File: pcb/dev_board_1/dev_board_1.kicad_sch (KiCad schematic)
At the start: 54 parts, among them SW1 SW_DIP_x01, SW10 SW_DIP_x01, SW11 SW_DIP_x01, SW12 SW_DIP_x01, SW13 SW_DIP_x01, SW14 SW_DIP_x01, SW15 SW_DIP_x01, SW16 SW_DIP_x01, SW17 SW_DIP_x01, SW18 SW_DIP_x01, SW19 SW_DIP_x01, SW2 SW_DIP_x01, SW20 SW_DIP_x01, SW21 SW_DIP_x01, SW22 SW_DIP_x01, SW23 SW_DIP_x01, SW24 SW_DIP_x01, SW3 SW_DIP_x01, SW4 SW_DIP_x01, SW5 SW_DIP_x01, SW6 SW_DIP_x01, SW7 SW_DIP_x01, SW8 SW_DIP_x01, SW9 SW_DIP_x01, U1 ili9341_touch_3.2, U2 LD3985M33R_SOT23, U3 STM32F427ZGTx, U4 MT48LC16M16A2TG

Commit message: add display
Add ili9341 display whit parallel interface
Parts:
- added SW25, SW26: SW_Push, Button_Switch_SMD:SW_SPST_SKQG_WithoutStem, symbol Switch:SW_Push
- added U5: ~, my_lib:ili9486_16bit_3.2, symbol my_lib:ili9341_touch_sd_16bit
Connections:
- net +3.3V: now also U3.108 (VDD), U3.121 (VDD), U3.131 (VDD), U3.144 (VDD), U3.17 (VDD), U3.30 (VDD), U3.33 (VDDA), U3.39 (VDD), U3.52 (VDD), U3.62 (VDD), U3.72 (VDD), U3.84 (VDD), U3.95 (VDD), U4.1 (VDD), U4.14 (VDD), U4.27 (VDD), U4.3 (VDDQ), U4.43 (VDDQ), U4.49 (VDDQ), U4.9 (VDDQ), U5.24 (VCC), U5.25 (VCC)
- net GND: now also U3.107 (VSS), U3.120 (VSS), U3.130 (VSS), U3.16 (VSS), U3.31 (VSSA), U3.38 (VSS), U3.51 (VSS), U3.61 (VSS), U3.83 (VSS), U3.94 (VSS), U4.12 (VSSQ), U4.28 (VSS), U4.41 (VSS), U4.46 (VSSQ), U4.52 (VSSQ), U4.54 (VSS), U4.6 (VSSQ), U5.26 (GND), U5.27 (GND)
- net cs_touch: now also U5.33 (~{CS_touch}); no longer U1.11 (~{CS_touch})
- net irg_touch: no longer U1.14 (IRQ_touch)
- net miso_touch: now also U5.29 (MISO_touch); no longer U1.13 (MISO_touch)
- net mosi_touch: now also U5.30 (MOSI_touch); no longer U1.12 (MOSI_touch)
- net sck_touch: now also U5.34 (SCK_touch); no longer U1.10 (SCK_touch)
- net FMC_NOE: now reaches U3.118 (PD4)
- net FMC_NOE: now also U5.4 (RD)
- net FMC_NWE: now reaches U3.119 (PD5)
- net FMC_NWE: now also U5.3 (WR)
- net FMC_NE1: now reaches U3.123 (PD7)
- net FMC_NE1: now also U5.1 (~{CS_display})
- net FMC_A16: now reaches U3.80 (PD11)
- net FMC_A16: now also U5.2 (D/~{C}_display)
- net sdram_A0 renamed FMC_A0
- net sdram_A1 renamed FMC_A1
- net sdram_A10 renamed FMC_A10
- net sdram_A11 renamed FMC_A11
- net sdram_A12 renamed FMC_A12
- net sdram_A2 renamed FMC_A2
- net sdram_A3 renamed FMC_A3
- net sdram_A4 renamed FMC_A4
- net sdram_A5 renamed FMC_A5
- net sdram_A6 renamed FMC_A6
- net sdram_A7 renamed FMC_A7
- net sdram_A8 renamed FMC_A8
- net sdram_A9 renamed FMC_A9
- net sdram_BA0 renamed FMC_BA0
- net sdram_BA1 renamed FMC_BA1
- net sdram_CKE renamed FMC_CKE
- net sdram_CLK renamed FMC_CLK
- net sdram_D0 renamed FMC_D0
- net FMC_D0: now also U5.6 (DB0)
- net sdram_D1 renamed FMC_D1
- net FMC_D1: now also U5.7 (DB1)
- net sdram_D10 renamed FMC_D10
- net FMC_D10: now also U5.16 (DB10)
- net sdram_D11 renamed FMC_D11
- net FMC_D11: now also U5.17 (DB11)
- net sdram_D12 renamed FMC_D12
- net FMC_D12: now also U5.18 (DB12)
- net sdram_D13 renamed FMC_D13
- net FMC_D13: now also U5.19 (DB13)
- net sdram_D14 renamed FMC_D14
- net FMC_D14: now also U5.20 (DB14)
- net sdram_D15 renamed FMC_D15
- net FMC_D15: now also U5.21 (DB15)
- net sdram_D2 renamed FMC_D2
- net FMC_D2: now also U5.8 (DB2)
- net sdram_D3 renamed FMC_D3
- net FMC_D3: now also U5.9 (DB3)
- net sdram_D4 renamed FMC_D4
- net FMC_D4: now also U5.10 (DB4)
- net sdram_D5 renamed FMC_D5
- net FMC_D5: now also U5.11 (DB5)
- net sdram_D6 renamed FMC_D6
- net FMC_D6: now also U5.12 (DB6)
- net sdram_D7 renamed FMC_D7
- net FMC_D7: now also U5.13 (DB7)
- net sdram_D8 renamed FMC_D8
- net FMC_D8: now also U5.14 (DB8)
- net sdram_D9 renamed FMC_D9
- net FMC_D9: now also U5.15 (DB9)
- net sdram_DQMH renamed FMC_DQMH
- net sdram_DQML renamed FMC_DQML
- net sdram_~{CAS} renamed FMC_~{CAS}
- net sdram_~{CS} renamed FMC_~{CS}
- net sdram_~{RAS} renamed FMC_~{RAS}
- net sdram_~{WE} renamed FMC_~{WE}
- new net LCD_LED: U5.23 (LED)
- new net LCD_RESET: U5.5 (RESET)
- new net irq_touch: U5.31 (IRQ_touch)

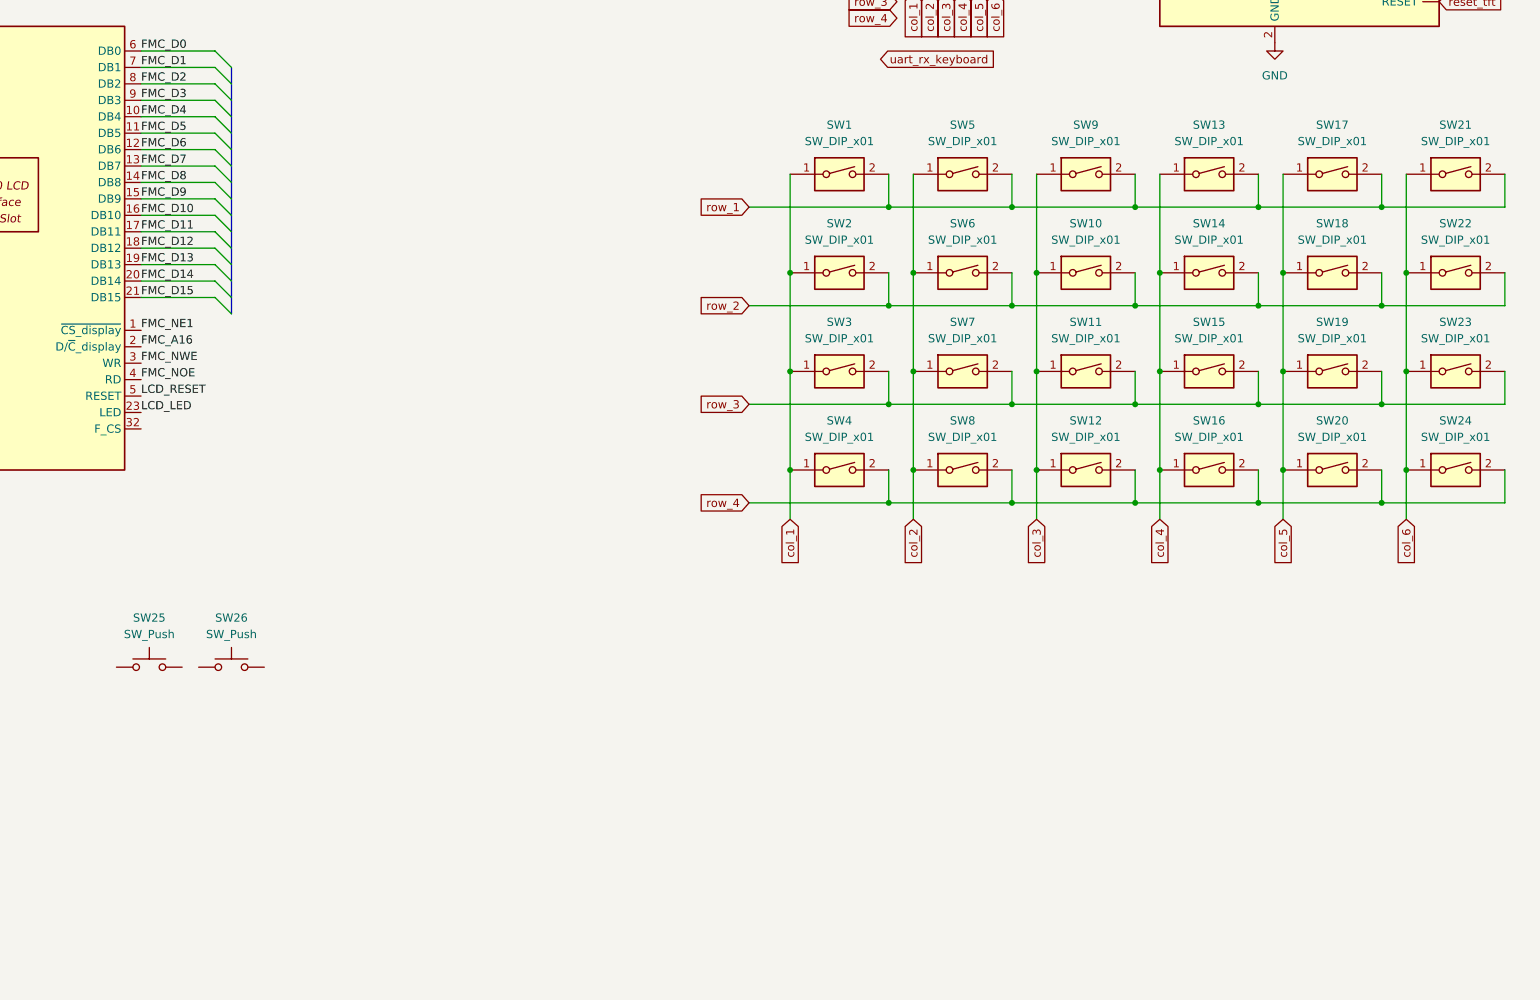
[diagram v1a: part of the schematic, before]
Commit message: New buttons for calc keyboard
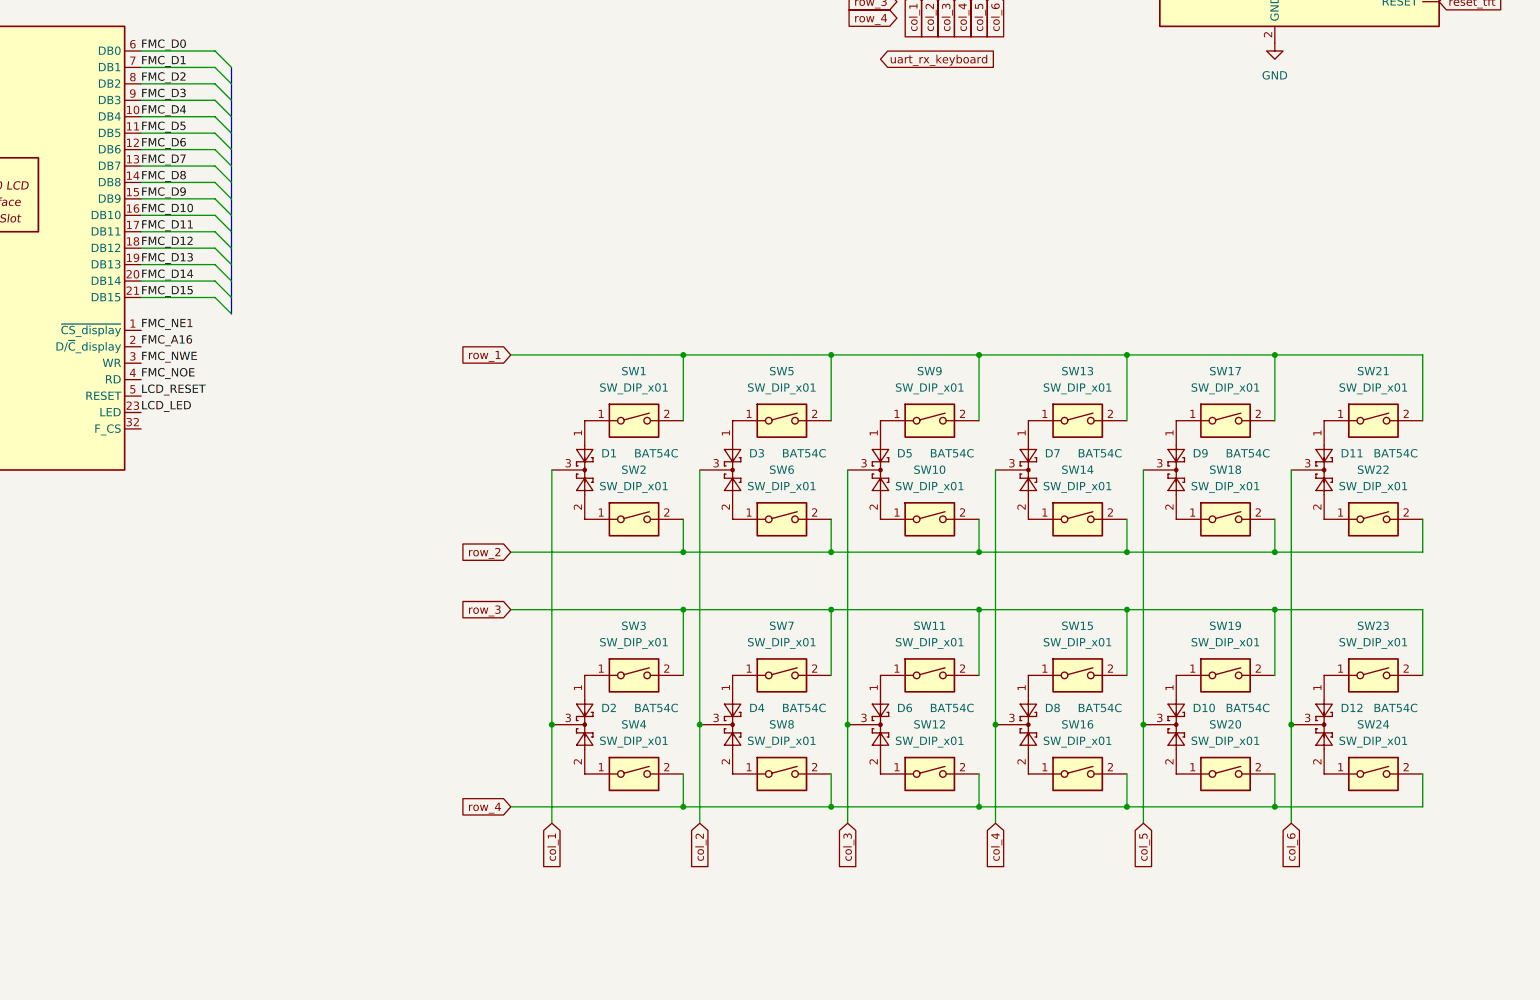
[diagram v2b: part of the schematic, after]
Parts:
- removed SW25, SW26: SW_Push, Button_Switch_SMD:SW_SPST_SKQG_WithoutStem, symbol Switch:SW_Push
- added D1, D10, D11, D12, D2, D3, D4, D5, D6, D7, D8, D9: BAT54C, Package_TO_SOT_SMD:SOT-23, symbol Diode:BAT54C
- SW1, SW10, SW11, SW12, SW13, SW14, SW15, SW16, SW17, SW18, SW19, SW2, SW20, SW21, SW22, SW23, SW24, SW3, SW4, SW5, SW6, SW7, SW8, SW9: footprint my_lib:btn_8x8 -> Button_Switch_SMD:SW_SPST_SKQG_WithoutStem
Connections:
- net col_1: now also D1.3, D2.3; no longer SW1.1, SW2.1, SW3.1, SW4.1
- net col_2: now also D3.3, D4.3; no longer SW5.1, SW6.1, SW7.1, SW8.1
- net col_3: now also D5.3, D6.3; no longer SW10.1, SW11.1, SW12.1, SW9.1
- net col_4: now also D7.3, D8.3; no longer SW13.1, SW14.1, SW15.1, SW16.1
- net col_5: now also D10.3, D9.3; no longer SW17.1, SW18.1, SW19.1, SW20.1
- net col_6: now also D11.3, D12.3; no longer SW21.1, SW22.1, SW23.1, SW24.1
- new net: D3.1, SW5.1
- new net: D11.1, SW21.1
- new net: D7.1, SW13.1
- new net: D10.1, SW19.1
- new net: D9.2, SW18.1
- new net: D1.1, SW1.1
- new net: D11.2, SW22.1
- new net: D1.2, SW2.1
- new net: D10.2, SW20.1
- new net: D12.1, SW23.1
- new net: D12.2, SW24.1
- new net: D6.1, SW11.1
- new net: D6.2, SW12.1
- new net: D7.2, SW14.1
- new net: D2.1, SW3.1
- new net: D2.2, SW4.1
- new net: D9.1, SW17.1
- new net: D4.2, SW8.1
- new net: D8.1, SW15.1
- new net: D8.2, SW16.1
- new net: D4.1, SW7.1
- new net: D3.2, SW6.1
- new net: D5.2, SW10.1
- new net: D5.1, SW9.1
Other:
- moved on the sheet: SW1, SW10, SW11, SW12, SW13, SW14, SW15, SW16, SW17, SW18, SW19, SW2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

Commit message: add another trace for sdram
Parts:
- removed U1: ili9341_touch_3.2, my_lib:ili9341_3.2, symbol my_lib:ili9341_touch_3.2
- added C18, C27, C28, C29, C30, C31, C32, C33, C34, C35, C36, C37, C38, C39, C40, C41, C42, C43, C44, C45: 100nF, Capacitor_SMD:C_0603_1608Metric_Pad1.08x0.95mm_HandSolder, symbol Device:C
- added C26: 10mkF, Capacitor_SMD:C_0603_1608Metric_Pad1.08x0.95mm_HandSolder, symbol Device:C
- added U6: STM32F427ZGTx, Package_QFP:LQFP-144_20x20mm_P0.5mm, symbol MCU_ST_STM32F4:STM32F427ZGTx
- added U7: MT48LC16M16A2TG, Package_SO:TSOP-II-54_22.2x10.16mm_P0.8mm, symbol Memory_RAM:MT48LC16M16A2TG
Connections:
- net +3.3V: now also C18.1, C26.1, C27.1, C28.1, C29.1, C30.1, C31.1, C32.1, C33.1, C34.1, C35.1, C36.1, C37.1, C38.1, C39.1, C40.1, C41.1, C42.1, C43.1, C44.1, C45.1, U6.108 (VDD), U6.121 (VDD), U6.131 (VDD), U6.144 (VDD), U6.17 (VDD), U6.30 (VDD), U6.33 (VDDA), U6.39 (VDD), U6.52 (VDD), U6.62 (VDD), U6.72 (VDD), U6.84 (VDD), U6.95 (VDD), U7.1 (VDD), U7.14 (VDD), U7.27 (VDD), U7.3 (VDDQ), U7.43 (VDDQ), U7.49 (VDDQ), U7.9 (VDDQ)
- net GND: now also C18.2, C26.2, C27.2, C28.2, C29.2, C30.2, C31.2, C32.2, C33.2, C34.2, C35.2, C36.2, C37.2, C38.2, C39.2, C40.2, C41.2, C42.2, C43.2, C44.2, C45.2, U6.107 (VSS), U6.120 (VSS), U6.130 (VSS), U6.16 (VSS), U6.31 (VSSA), U6.38 (VSS), U6.51 (VSS), U6.61 (VSS), U6.83 (VSS), U6.94 (VSS), U7.12 (VSSQ), U7.28 (VSS), U7.41 (VSS), U7.46 (VSSQ), U7.52 (VSSQ), U7.54 (VSS), U7.6 (VSSQ)
- net RCC1: now reaches U3.23 (PH0)
- net RCC2: now reaches U3.24 (PH1)
- new net TEST_1_FMC_A0: U6.10 (PF0), U7.23 (A0)
- new net TEST_1_FMC_A1: U6.11 (PF1), U7.24 (A1)
- new net TEST_1_FMC_A10: U6.56 (PG0), U7.22 (A10)
- new net TEST_1_FMC_A11: U6.57 (PG1), U7.35 (A11)
- new net TEST_1_FMC_A12: U6.87 (PG2), U7.36 (A12)
- new net TEST_1_FMC_A2: U6.12 (PF2), U7.25 (A2)
- new net TEST_1_FMC_A3: U6.13 (PF3), U7.26 (A3)
- new net TEST_1_FMC_A4: U6.14 (PF4), U7.29 (A4)
- new net TEST_1_FMC_A5: U6.15 (PF5), U7.30 (A5)
- new net TEST_1_FMC_A6: U6.50 (PF12), U7.31 (A6)
- new net TEST_1_FMC_A7: U6.53 (PF13), U7.32 (A7)
- new net TEST_1_FMC_A8: U6.54 (PF14), U7.33 (A8)
- new net TEST_1_FMC_A9: U6.55 (PF15), U7.34 (A9)
- new net TEST_1_FMC_BA0: U6.89 (PG4), U7.20 (BA0)
- new net TEST_1_FMC_BA1: U6.90 (PG5), U7.21 (BA1)
- new net TEST_1_FMC_CKE: U6.29 (PC3), U7.37 (CKE)
- new net TEST_1_FMC_CLK: U6.93 (PG8), U7.38 (CLK)
- new net TEST_1_FMC_D0: U6.85 (PD14), U7.2 (DQ0)
- new net TEST_1_FMC_D1: U6.86 (PD15), U7.4 (DQ1)
- new net TEST_1_FMC_D10: U6.66 (PE13), U7.45 (DQ10)
- new net TEST_1_FMC_D11: U6.67 (PE14), U7.47 (DQ11)
- new net TEST_1_FMC_D12: U6.68 (PE15), U7.48 (DQ12)
- new net TEST_1_FMC_D13: U6.77 (PD8), U7.50 (DQ13)
- new net TEST_1_FMC_D14: U6.78 (PD9), U7.51 (DQ14)
- new net TEST_1_FMC_D15: U6.79 (PD10), U7.53 (DQ15)
- new net TEST_1_FMC_D2: U6.114 (PD0), U7.5 (DQ2)
- new net TEST_1_FMC_D3: U6.115 (PD1), U7.7 (DQ3)
- new net TEST_1_FMC_D4: U6.58 (PE7), U7.8 (DQ4)
- new net TEST_1_FMC_D5: U6.59 (PE8), U7.10 (DQ5)
- new net TEST_1_FMC_D6: U6.60 (PE9), U7.11 (DQ6)
- new net TEST_1_FMC_D7: U6.63 (PE10), U7.13 (DQ7)
- new net TEST_1_FMC_D8: U6.64 (PE11), U7.42 (DQ8)
- new net TEST_1_FMC_D9: U6.65 (PE12), U7.44 (DQ9)
- new net TEST_1_FMC_DQMH: U6.142 (PE1), U7.39 (DQMH)
- new net TEST_1_FMC_DQML: U6.141 (PE0), U7.15 (DQML)
- new net TEST_1_FMC_~{CAS}: U6.132 (PG15), U7.17 (~{CAS})
- new net TEST_1_FMC_~{CS}: U6.28 (PC2), U7.19 (~{CS})
- new net TEST_1_FMC_~{RAS}: U6.49 (PF11), U7.18 (~{RAS})
- new net TEST_1_FMC_~{WE}: U6.26 (PC0), U7.16 (~{WE})
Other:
- moved on the sheet: C1, C10, C11, C12, C13, C14, C15, C16, C17, C19, C2, C20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

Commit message: add track to display and usb c
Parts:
- removed C10, C11, C12, C13, C14, C19, C20, C21, C22, C23, C24, C25, C3, C4, C5, C6, C7, C8, C9: 100nF, Capacitor_SMD:C_0603_1608Metric_Pad1.08x0.95mm_HandSolder, symbol Device:C
- removed U3: STM32F427ZGTx, Package_QFP:LQFP-144_20x20mm_P0.5mm, symbol MCU_ST_STM32F4:STM32F427ZGTx
- removed U4: MT48LC16M16A2TG, Package_SO:TSOP-II-54_22.2x10.16mm_P0.8mm, symbol Memory_RAM:MT48LC16M16A2TG
- added J1: Conn_01x03, Connector_PinHeader_2.54mm:PinHeader_1x03_P2.54mm_Vertical, symbol Connector_Generic:Conn_01x03
- added P1: USB_C_Plug_USB2.0, Connector_USB:USB_C_Receptacle_HRO_TYPE-C-31-M-12, symbol Connector:USB_C_Plug_USB2.0
- added R3, R6: 5.1k, Resistor_SMD:R_0603_1608Metric_Pad0.98x0.95mm_HandSolder, symbol Device:R
- added R4, R7: 20R, Resistor_SMD:R_0603_1608Metric_Pad0.98x0.95mm_HandSolder, symbol Device:R
- added R5: 1k, Resistor_SMD:R_0603_1608Metric_Pad0.98x0.95mm_HandSolder, symbol Device:R
- added Y1: Crystal, Crystal:Crystal_SMD_2520-4Pin_2.5x2.0mm, symbol Device:Crystal
- C1: value 10mkF -> 20pF
- C2: value 100nF -> 20pF
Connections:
- net TEST_1_FMC_A0 is gone; now on net FMC_A0: U6.10 (PF0), U7.23 (A0)
- net TEST_1_FMC_A1 is gone; now on net FMC_A1: U6.11 (PF1), U7.24 (A1)
- net TEST_1_FMC_A10 is gone; now on net FMC_A10: U6.56 (PG0), U7.22 (A10)
- net TEST_1_FMC_A11 is gone; now on net FMC_A11: U6.57 (PG1), U7.35 (A11)
- net TEST_1_FMC_A12 is gone; now on net FMC_A12: U6.87 (PG2), U7.36 (A12)
- net TEST_1_FMC_A2 is gone; now on net FMC_A2: U6.12 (PF2), U7.25 (A2)
- net TEST_1_FMC_A3 is gone; now on net FMC_A3: U6.13 (PF3), U7.26 (A3)
- net TEST_1_FMC_A4 is gone; now on net FMC_A4: U6.14 (PF4), U7.29 (A4)
- net TEST_1_FMC_A5 is gone; now on net FMC_A5: U6.15 (PF5), U7.30 (A5)
- net TEST_1_FMC_A6 is gone; now on net FMC_A6: U6.50 (PF12), U7.31 (A6)
- net TEST_1_FMC_A7 is gone; now on net FMC_A7: U6.53 (PF13), U7.32 (A7)
- net TEST_1_FMC_A8 is gone; now on net FMC_A8: U6.54 (PF14), U7.33 (A8)
- net TEST_1_FMC_A9 is gone; now on net FMC_A9: U6.55 (PF15), U7.34 (A9)
- net TEST_1_FMC_BA0 is gone; now on net FMC_BA0: U6.89 (PG4), U7.20 (BA0)
- net TEST_1_FMC_BA1 is gone; now on net FMC_BA1: U6.90 (PG5), U7.21 (BA1)
- net TEST_1_FMC_CKE is gone; now on net FMC_CKE: U6.29 (PC3), U7.37 (CKE)
- net TEST_1_FMC_CLK is gone; now on net FMC_CLK: U6.93 (PG8), U7.38 (CLK)
- net TEST_1_FMC_D0 is gone; now on net FMC_D0: U6.85 (PD14), U7.2 (DQ0)
- net TEST_1_FMC_D1 is gone; now on net FMC_D1: U6.86 (PD15), U7.4 (DQ1)
- net TEST_1_FMC_D10 is gone; now on net FMC_D10: U6.66 (PE13), U7.45 (DQ10)
- net TEST_1_FMC_D11 is gone; now on net FMC_D11: U6.67 (PE14), U7.47 (DQ11)
- net TEST_1_FMC_D12 is gone; now on net FMC_D12: U6.68 (PE15), U7.48 (DQ12)
- net TEST_1_FMC_D13 is gone; now on net FMC_D13: U6.77 (PD8), U7.50 (DQ13)
- net TEST_1_FMC_D14 is gone; now on net FMC_D14: U6.78 (PD9), U7.51 (DQ14)
- net TEST_1_FMC_D15 is gone; now on net FMC_D15: U6.79 (PD10), U7.53 (DQ15)
- net TEST_1_FMC_D2 is gone; now on net FMC_D2: U6.114 (PD0), U7.5 (DQ2)
- net TEST_1_FMC_D3 is gone; now on net FMC_D3: U6.115 (PD1), U7.7 (DQ3)
- net TEST_1_FMC_D4 is gone; now on net FMC_D4: U6.58 (PE7), U7.8 (DQ4)
- net TEST_1_FMC_D5 is gone; now on net FMC_D5: U6.59 (PE8), U7.10 (DQ5)
- net TEST_1_FMC_D6 is gone; now on net FMC_D6: U6.60 (PE9), U7.11 (DQ6)
- net TEST_1_FMC_D7 is gone; now on net FMC_D7: U6.63 (PE10), U7.13 (DQ7)
- net TEST_1_FMC_D8 is gone; now on net FMC_D8: U6.64 (PE11), U7.42 (DQ8)
- net TEST_1_FMC_D9 is gone; now on net FMC_D9: U6.65 (PE12), U7.44 (DQ9)
- net TEST_1_FMC_DQMH is gone; now on net FMC_DQMH: U6.142 (PE1), U7.39 (DQMH)
- net TEST_1_FMC_DQML is gone; now on net FMC_DQML: U6.141 (PE0), U7.15 (DQML)
- net TEST_1_FMC_~{CAS} is gone; now on net FMC_~{CAS}: U6.132 (PG15), U7.17 (~{CAS})
- net TEST_1_FMC_~{CS} is gone; now on net FMC_~{CS}: U6.28 (PC2), U7.19 (~{CS})
- net TEST_1_FMC_~{RAS} is gone; now on net FMC_~{RAS}: U6.49 (PF11), U7.18 (~{RAS})
- net TEST_1_FMC_~{WE} is gone; now on net FMC_~{WE}: U6.26 (PC0), U7.16 (~{WE})
- net +3.3V: now also R5.2; no longer C1.1, C2.1
- net +5V: now also P1.A4 (VBUS), P1.A9 (VBUS), P1.B4 (VBUS), P1.B9 (VBUS)
- net FMC_A16: now also U6.80 (PD11)
- net FMC_NE1: now also U6.123 (PD7)
- net FMC_NOE: now also U6.118 (PD4)
- net FMC_NWE: now also U6.119 (PD5)
- net GND: now also J1.1 (Pin_1), P1.A1 (GND), P1.A12 (GND), P1.B1 (GND), P1.B12 (GND), R3.1, R6.1
- net miso_touch: now also U6.42 (PA6)
- net mosi_touch: now also U6.43 (PA7)
- net sck_touch: now also U6.41 (PA5)
- net USB_D-: now reaches U6.103 (PA11)
- net USB_D-: now also R4.1
- net USB_D+: now reaches U6.104 (PA12)
- net USB_D+: now also R7.1
- net SWDIO: now reaches U6.105 (PA13)
- net SWDIO: now also J1.3 (Pin_3)
- net SWCLK: now reaches U6.109 (PA14)
- net SWCLK: now also J1.2 (Pin_2)
- net osc1: now reaches U6.23 (PH0)
- net osc1: now also C2.1, Y1.2
- net osc2: now reaches U6.24 (PH1)
- net osc2: now also C1.1, Y1.1
- new net: P1.A5 (CC), R3.2
- new net: P1.A6 (D+), R5.1, R7.2
- new net: P1.A7 (D-), R4.2
- new net: P1.B5 (VCONN), R6.2
- no-connect marks 0 -> 1

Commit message: place buttons
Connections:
- net LCD_RESET: now also U6.110 (PA15)
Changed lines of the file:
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@@
+    (effects (font (size 1.27 1.27)) (justify left bottom))
+  )
+  (label "LCD_RESET" (at 233.68 242.57 0) (fields_autoplaced)
     (effects (font (size 1.27 1.27)) (justify left bottom))
   )
